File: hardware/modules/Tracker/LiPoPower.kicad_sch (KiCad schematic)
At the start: 70 parts, among them J103 Battery, J104 Temp&Heater, J105 Ext Switch, J106 LiPo, Q101 Q_NMOS_GSD, Q102 Q_NMOS_GSD, Q103 Q_PMOS_GSD, Q104 Q_PMOS_GSD, Q105 Q_PNP_BEC, Q106 Q_PNP_BEC, Q107 Q_PMOS_GSD, Q108 Q_NPN_BEC, Q109 Q_PMOS_GSD, SW102 Power Switch, U107 MCP73871-1CC, U108 INA226, U109 INA226, U110 TPS63070RNMR, U111 INA226

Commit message: 広い部分のビアはあとまわしにしました．許せるエラー以外はつぶしたと思います．
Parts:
- LED101, LED102, LED103, LED104, LED105: footprint LED_SMD:LED_0603_1608Metric -> LED_SMD:LED_0805_2012Metric
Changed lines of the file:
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@@
 			)
 		)
-		(property "Footprint" "LED_SMD:LED_0603_1608Metric"
+		(property "Footprint" "LED_SMD:LED_0805_2012Metric"
 			(at 49.53 43.18 0)
 			(effects
@@
 			)
 		)
-		(property "Footprint" "LED_SMD:LED_0603_1608Metric"
+		(property "Footprint" "LED_SMD:LED_0805_2012Metric"
 			(at 277.495 49.53 0)
 			(effects
@@
 			)
 		)
-		(property "Footprint" "LED_SMD:LED_0603_1608Metric"
+		(property "Footprint" "LED_SMD:LED_0805_2012Metric"
 			(at 118.745 168.275 0)
 			(effects
@@
 			)
 		)
-		(property "Footprint" "LED_SMD:LED_0603_1608Metric"
+		(property "Footprint" "LED_SMD:LED_0805_2012Metric"
 			(at 31.115 180.975 0)
 			(effects
@@
 			)
 		)
-		(property "Footprint" "LED_SMD:LED_0603_1608Metric"
+		(property "Footprint" "LED_SMD:LED_0805_2012Metric"
 			(at 29.845 113.03 0)
 			(effects

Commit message: 細部の変更
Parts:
- R117, R118, R120, R121, R122, R124, R125, R126, R128, R134: LCSC C25530 -> C25741
- R130, R133, R137: LCSC C247588 -> C247602
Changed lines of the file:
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@@
 			)
 		)
-		(property "LCSC" "C25530"
+		(property "LCSC" "C25741"
 			(at 64.77 81.915 0)
 			(effects
@@
 			)
 		)
-		(property "LCSC" "C25530"
+		(property "LCSC" "C25741"
 			(at 75.565 51.435 0)
 			(effects
@@
 			)
 		)
-		(property "LCSC" "C25530"
+		(property "LCSC" "C25741"
 			(at 59.055 43.18 0)
 			(effects
@@
 			)
 		)
-		(property "LCSC" "C247588"
+		(property "LCSC" "C247602"
 			(at 174.625 110.49 0)
 			(effects
@@
 			)
 		)
-		(property "LCSC" "C25530"
+		(property "LCSC" "C25741"
 			(at 57.15 68.58 0)
 			(effects
@@
 			)
 		)
-		(property "LCSC" "C247588"
+		(property "LCSC" "C247602"
 			(at 267.335 38.735 0)
 			(effects
@@
 			)
 		)
-		(property "LCSC" "C247588"
+		(property "LCSC" "C247602"
 			(at 125.73 38.735 0)
 			(effects
@@
 			)
 		)
-		(property "LCSC" "C25530"
+		(property "LCSC" "C25741"
 			(at 212.09 52.07 0)
 			(effects
@@
 			)
 		)
-		(property "LCSC" "C25530"
+		(property "LCSC" "C25741"
 			(at 75.565 62.865 0)
 			(effects
@@
 			)
 		)
-		(property "LCSC" "C25530"
+		(property "LCSC" "C25741"
 			(at 45.72 123.19 0)
 			(effects
@@
 			)
 		)
-		(property "LCSC" "C25530"
+		(property "LCSC" "C25741"
 			(at 42.545 63.5 0)
 			(effects
@@
 			)
 		)
-		(property "LCSC" "C25530"
+		(property "LCSC" "C25741"
 			(at 101.6 167.64 0)
 			(effects
@@
 			)
 		)
-		(property "LCSC" "C25530"
+		(property "LCSC" "C25741"
 			(at 50.8 107.95 0)
 			(effects

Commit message: 抵抗等変更しました
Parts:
- R116, R136: value 470k -> 47k; LCSC C25790 -> C25792
- R117: value 100k -> 10k; LCSC C25741 -> C25744
- R132: value 470k -> 330k; LCSC C25790 -> C23137
- R135: value 150k -> 15k; LCSC C25755 -> C25756
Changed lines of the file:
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@@
 			)
 		)
-		(property "Value" "470k"
+		(property "Value" "47k"
 			(at 40.64 52.07 90)
 			(effects
@@
 			)
 		)
-		(property "LCSC" "C25790"
+		(property "LCSC" "C25792"
 			(at 42.545 52.07 0)
 			(effects
@@
 			)
 		)
-		(property "Value" "470k"
+		(property "Value" "47k"
 			(at 223.52 42.545 90)
 			(effects
@@
 			)
 		)
-		(property "LCSC" "C25790"
+		(property "LCSC" "C25792"
 			(at 223.52 44.45 0)
 			(effects
@@
 			)
 		)
-		(property "Value" "470k"
+		(property "Value" "330k"
 			(at 146.685 64.77 0)
 			(effects
@@
 			)
 		)
-		(property "LCSC" "C25790"
+		(property "LCSC" "C23137"
 			(at 153.67 63.5 0)
 			(effects
@@
 			)
 		)
-		(property "Value" "150k"
+		(property "Value" "15k"
 			(at 220.98 50.165 0)
 			(effects
@@
 			)
 		)
-		(property "LCSC" " C25755"
+		(property "LCSC" " C25756"
 			(at 219.075 48.895 0)
 			(effects
@@
 			)
 		)
-		(property "Value" "100k"
+		(property "Value" "10k"
 			(at 40.64 63.5 90)
 			(effects
@@
 			)
 		)
-		(property "LCSC" "C25741"
+		(property "LCSC" "C25744"
 			(at 42.545 63.5 0)
 			(effects

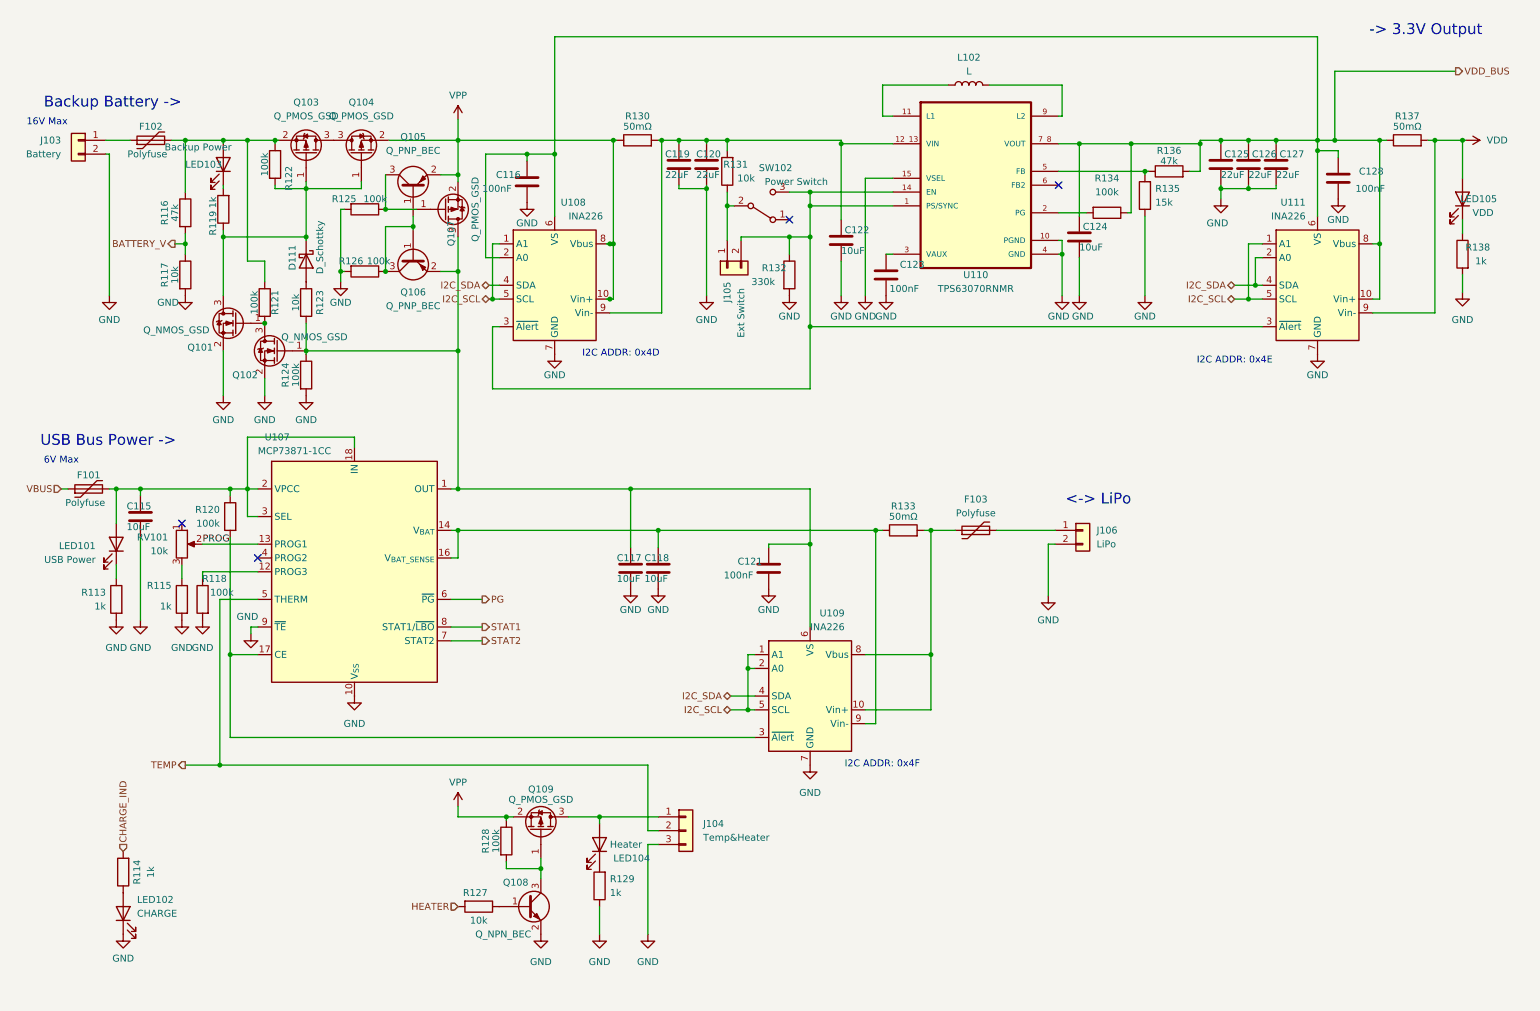
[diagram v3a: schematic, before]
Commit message: GPSのfootprint差し替え，lipo側INA(0x4F)のVSをVDDにつないだ.
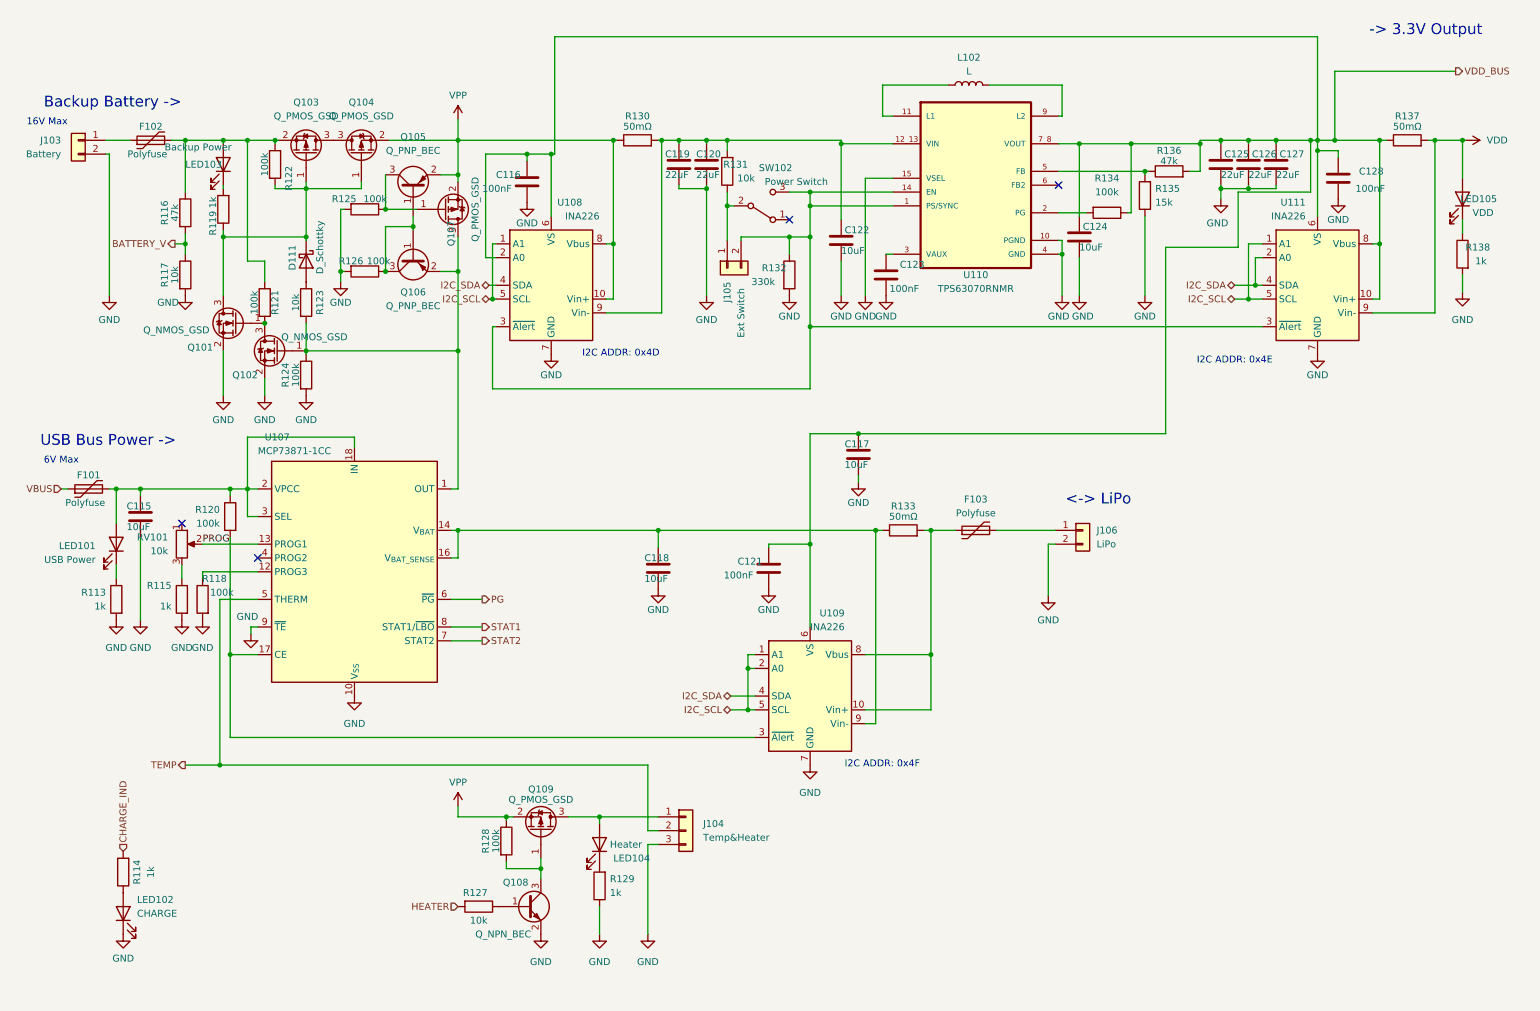
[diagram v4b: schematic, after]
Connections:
- net VDD_BUS: now also C117.1, C121.1, U109.6 (VS)
- net at Q102.1 (G), Q106.2 (E), Q107.3 (D)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: no longer C117.1, C121.1, U109.6 (VS)
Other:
- moved on the sheet: C117, U108

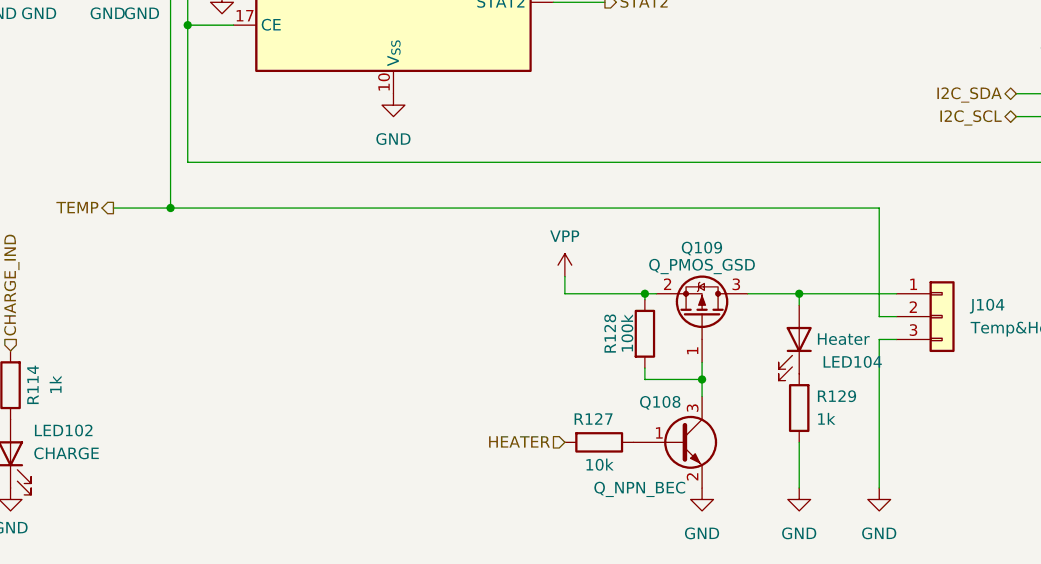
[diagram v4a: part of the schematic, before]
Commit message: Igniteコンポーネントの作成とTrackerモジュールの修正
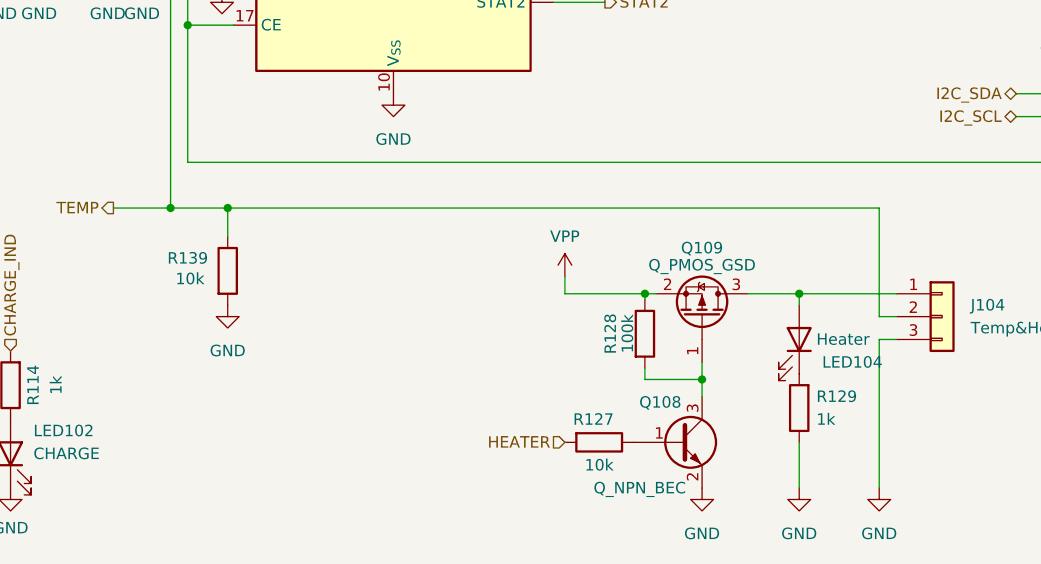
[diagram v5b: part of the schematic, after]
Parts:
- added R139: 10k, Resistor_SMD:R_0402_1005Metric, symbol Device:R
- R135: LCSC C25756 -> C25756
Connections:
- net GND: now also R139.2
- net TEMP: now also R139.1
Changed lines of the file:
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@@
 	)
 	(junction
+		(at 55.245 153.67)
+		(diameter 0)
+		(color 0 0 0 0)
+	)
+	(junction
 		(at 219.075 44.45)
 		(diameter 0)
@@
 	(wire
 		(pts
-			(xy 48.895 153.67) (xy 127.635 153.67)
+			(xy 48.895 153.67) (xy 55.245 153.67)
 		)
 		(stroke
@@
 	(wire
 		(pts
+			(xy 55.245 153.67) (xy 127.635 153.67)
+		)
+		(stroke
+			(width 0)
+			(type default)
+		)
+	)
+	(wire
+		(pts
 			(xy 233.045 47.625) (xy 233.045 46.99)
 		)
@@
 	(wire
 		(pts
+			(xy 55.245 153.67) (xy 55.245 156.845)
+		)
+		(stroke
+			(width 0)
+			(type default)
+		)
+	)
+	(wire
+		(pts
 			(xy 34.29 102.87) (xy 50.8 102.87)
 		)
@@
 	)
 	(symbol
+		(lib_id "Device:R")
+		(at 55.245 160.655 0)
+		(unit 1)
+		(exclude_from_sim no)
+		(in_bom yes)
+		(on_board yes)
+		(dnp no)
+		(property "Reference" "R139"
+			(at 50.8 159.258 0)
+			(effects
+				(font
+					(size 1.27 1.27)
+				)
+			)
+		)
+		(property "Value" "10k"
+			(at 51.054 161.544 0)
+			(effects
+				(font
+					(size 1.27 1.27)
+				)
+			)
+		)
+		(property "Footprint" "Resistor_SMD:R_0402_1005Metric"
+			(at 53.467 160.655 90)
+			(effects
+				(font
+					(size 1.27 1.27)
+				)
+				(hide yes)
+			)
+		)
+		(property "Datasheet" "~"
+			(at 55.245 160.655 0)
+			(effects
+				(font
+					(size 1.27 1.27)
+				)
+				(hide yes)
+			)
+		)
+		(property "Description" ""
+			(at 55.245 160.655 0)
+			(effects
+				(font
+					(size 1.27 1.27)
+				)
+				(hide yes)
+			)
+		)
+		(property "LCSC" "C25744"
+			(at 55.245 160.655 0)
+			(effects
+				(font
+					(size 1.27 1.27)
+				)
+				(hide yes)
+			)
+		)
+		(pin "1"
+		)
+		(pin "2"
+		)
+		(instances
+			(project "Tracker"
+				(path "/485a01ee-6a57-485f-8e4c-0ef4d16d0717/b564a1a6-880f-4f3f-9b5e-b689a4514f2f"
+					(reference "R139")
+					(unit 1)
+				)
+			)
+		)
+	)
+	(symbol
 		(lib_id "Device:Q_NPN_BEC")
 		(at 105.41 179.705 0)
@@
 	)
 	(symbol
+		(lib_id "power:GND")
+		(at 55.245 164.465 0)
+		(unit 1)
+		(exclude_from_sim no)
+		(in_bom yes)
+		(on_board yes)
+		(dnp no)
+		(fields_autoplaced yes)
+		(property "Reference" "#PWR0176"
+			(at 55.245 170.815 0)
+			(effects
+				(font
+					(size 1.27 1.27)
+				)
+				(hide yes)
+			)
+		)
+		(property "Value" "GND"
+			(at 55.245 169.545 0)
+			(effects
+				(font
+					(size 1.27 1.27)
+				)
+			)
+		)
+		(property "Footprint" ""
+			(at 55.245 164.465 0)
+			(effects
+				(font
+					(size 1.27 1.27)
+				)
+				(hide yes)
+			)
+		)
+		(property "Datasheet" ""
+			(at 55.245 164.465 0)
+			(effects
+				(font
+					(size 1.27 1.27)
+				)
+				(hide yes)
+			)
+		)
+		(property "Description" ""
+			(at 55.245 164.465 0)
+			(effects
+				(font
+					(size 1.27 1.27)
+				)
+				(hide yes)
+			)
+		)
+		(pin "1"
+		)
+		(instances
+			(project "Tracker"
+				(path "/485a01ee-6a57-485f-8e4c-0ef4d16d0717/b564a1a6-880f-4f3f-9b5e-b689a4514f2f"
+					(reference "#PWR0176")
+					(unit 1)
+				)
+			)
+		)
+	)
+	(symbol
 		(lib_id "Device:Q_PNP_BEC")
 		(at 84.455 60.325 90)
@@
 			)
 		)
-		(property "LCSC" " C25756"
+		(property "LCSC" "C25756"
 			(at 219.075 48.895 0)
 			(effects

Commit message: Tracker諸々の修正
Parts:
- removed D111: D_Schottky, Diode_SMD:D_SOD-323, symbol Device:D_Schottky
- removed F102: Polyfuse, Fuse:Fuse_1206_3216Metric, symbol Device:Polyfuse
- removed LED103: Backup Power, LED_SMD:LED_0805_2012Metric, symbol Device:LED
- removed Q101, Q102: Q_NMOS_GSD, Package_TO_SOT_SMD:SOT-23-3, symbol Device:Q_NMOS_GSD
- removed Q103, Q104, Q107: Q_PMOS_GSD, Package_TO_SOT_SMD:SOT-23, symbol Device:Q_PMOS_GSD
- removed Q105, Q106: Q_PNP_BEC, Package_TO_SOT_SMD:SOT-23-3, symbol Device:Q_PNP_BEC
- removed R116: 47k, Resistor_SMD:R_0402_1005Metric, symbol Device:R
- removed R117, R123, R139: 10k, Resistor_SMD:R_0402_1005Metric, symbol Device:R
- removed R119: 1k, Resistor_SMD:R_0402_1005Metric, symbol Device:R
- removed R121, R122, R124, R125, R126: 100k, Resistor_SMD:R_0402_1005Metric, symbol Device:R
- added C702, C703: 10uF, Capacitor_SMD:C_0603_1608Metric, symbol Device:C
- added F702: Polyfuse, Fuse:Fuse_1206_3216Metric, symbol Device:Polyfuse
- added LED703: Backup, LED_SMD:LED_0805_2012Metric, symbol Device:LED
- added R706: 47k, Resistor_SMD:R_0402_1005Metric, symbol Device:R
- added R707, R710: 100k, Resistor_SMD:R_0402_1005Metric, symbol Device:R
- added R709: 1k, Resistor_SMD:R_0402_1005Metric, symbol Device:R
- added R715: 10k, Resistor_SMD:R_0402_1005Metric, symbol Device:R
- added U702: TPS2116DRL, Package_TO_SOT_SMD:SOT-583-8, symbol Power_Management:TPS2116DRL
- L701: renamed from L102; LCSC C3033018 -> C3033018
- R711: renamed from R128; value 100k -> 10k; LCSC C25741 -> C25744
- renumbered C115 to C701, C116 to C704, C117 to C705, C118 to C706, C119 to C707, C120 to C708, C121 to C709, C122 to C710, C123 to C711, C124 to C712, C125 to C713, C126 to C714, C127 to C715, C128 to C716, F101 to F701, F103 to F703, J103 to J701, J104 to J702, J105 to J703, J106 to J704, LED101 to LED701, LED102 to LED702, LED104 to LED704, LED105 to LED705, Q108 to Q701, Q109 to Q702, R113 to R701, R114 to R702, R115 to R703, R118 to R704, R120 to R705, R127 to R708, R129 to R712, R130 to R713, R131 to R714, R132 to R716, R133 to R717, R134 to R718, R135 to R719, R136 to R720, R137 to R721, R138 to R722, RV101 to RV701, SW102 to SW701, U107 to U701, U108 to U703, U109 to U704, U110 to U705, U111 to U706
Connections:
- net GND: now also C702.2, C703.2, R706.1, R710.2, R715.2, U702.1 (GND)
- net TEMP: now also R715.1
- net VDD_BUS: no longer C704.1, C705.1, C709.1, U703.2 (A0), U703.6 (VS), U704.6 (VS)
- net VPP: now also C704.1, C709.1, U703.2 (A0), U703.6 (VS), U704.6 (VS), LED703.2 (A), U702.2 (VOUT), U702.7 (VOUT)
- net at U701.1 (OUT), U701.20 (OUT): now also C705.1, C703.1, R707.1, U702.3 (VIN1), U702.5 (MODE)
- net at J701.1 (Pin_1): now also F702.1
- net at Q701.1 (B), R708.1: now also R710.1
- net VBUS renamed VUSB
- new net: C702.1, F702.2, U702.6 (VIN2)
- new net: R706.2, R707.2, U702.4 (PR1)
- new net: LED703.1 (K), R709.1
- new net ST: R709.2, U702.8 (ST)
- no-connect marks 4 -> 1
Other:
- note added: "コネクタあるいは プルダウン抵抗を選択"
- note removed: "16V Max"
- moved on the sheet: C701, C704, C705, C706, C707, C708, C709, C710, C711, C712, C713, C714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
